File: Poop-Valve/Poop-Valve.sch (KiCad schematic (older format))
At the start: 51 parts, among them J1 RaspberryPi, J10 Valve Sig, J11 Conn_01x02_Male, J12 Relays, J13 LEDs, J14 24VDC, J15 Sensor, J16 Grove LCD, J2 Valve, J3 Charger, J4 Override, J5 Ovr Switch, J6 Power, J7 12VDC, J8 Conn_01x02_Male, J9 Conn_01x02_Male, K1 Override Relays, K2 Polarity Reverse, K3 Enable Relays, K4 Relay_Module, K5 Direction Relays, K6 Polarity Reverse, Q1 2N2222, Q2 2N2222, SW1 Override, SW2 Emergency Override, SW2 SW_DPDT_x2, SW3 Open/Close, U1 Opened, U2 Closed, U3 Override, U4 MCP3008

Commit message: v1.1 replace valve connector
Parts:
- removed J2: Valve, symbol Connector:6P6C
- added J17: Valve, symbol Connector:Conn_01x05_Male
- added J2: Dongle, symbol Connector:Conn_01x05_Female
- J10: value Valve Sig -> O/C
- gave numbers to parts that had none: 1
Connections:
- net +12V: now reaches F1.2, J11.1 (Pin_1), J8.1 (Pin_1), J9.1 (Pin_1), K5.~ (VCC), K6.~ (VCC), SW2.3, SW3.1
- net +12V: now also J10.2 (Pin_2), J17.3 (Pin_3)
- net at R3.2, R6.2: now also J10.1 (Pin_1), J17.2 (Pin_2); no longer J10.3 (Pin_3)
- net at R2.2, R5.2: now also J10.3 (Pin_3), J17.1 (Pin_1); no longer J10.1 (Pin_1)
- new net: K1.~ (VCC), K2.~ (VCC), K3.~ (VCC), K4.~ (VCC), K5.~ (VCC), K6.~ (VCC)
- new net: K1.~ (VCC), K3.~ (VCC)
- new net: K3.~ (VCC), K6.~ (VCC)
- new net: K2.~ (VCC), K4.~ (VCC)
- new net: K4.~ (VCC), K5.~ (VCC)
- new net: J17.5 (Pin_5), K1.~ (VCC)
- new net: J17.4 (Pin_4), K2.~ (VCC)
- no-connect marks 36 -> 33
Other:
- note added: "Ovr"
- note added: "Run"
- note added: "SW2\nEmergency\nOverride"
- note added: "To valve"
- note added: "black/white"
- note removed: "Operate"
- note removed: "Override"
- note removed: "pin"
- moved on the sheet: J16

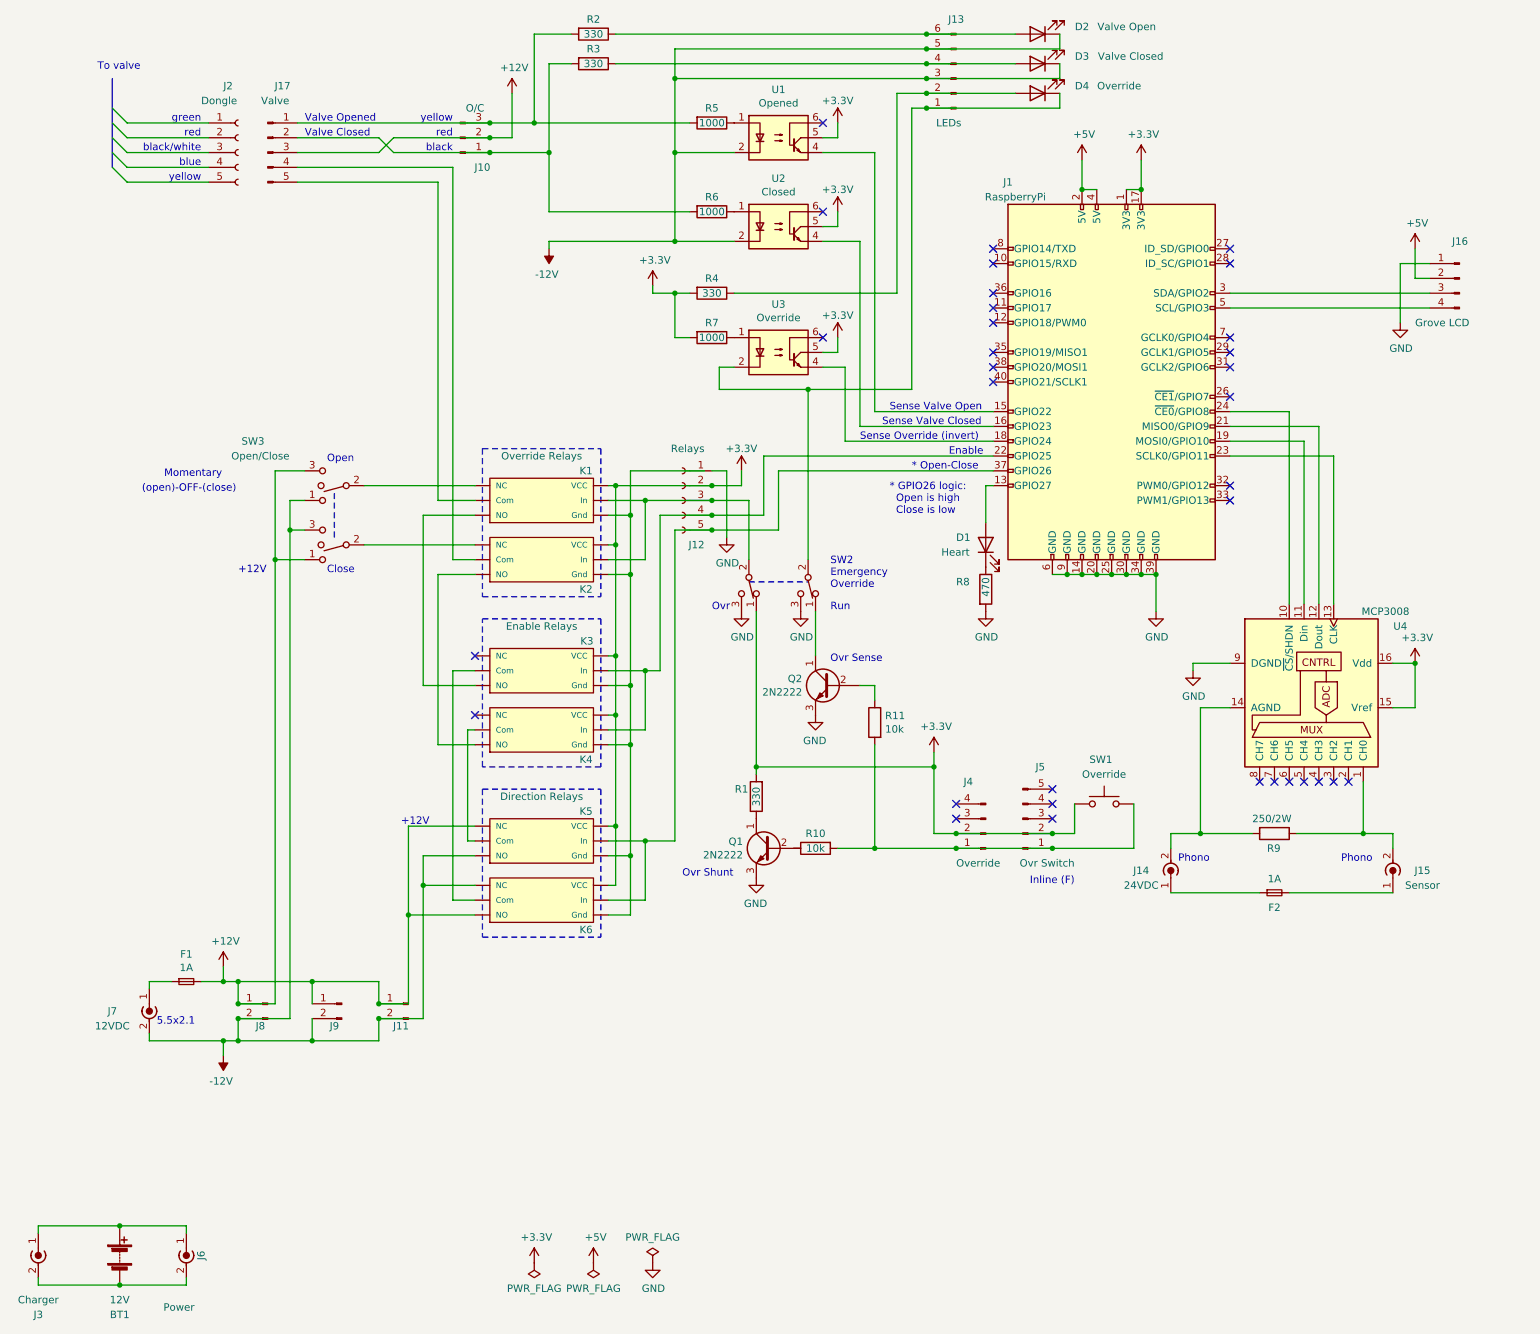
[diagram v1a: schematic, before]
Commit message: v1.2 reconfigure override relay to use 5V voltage divider; renumber parts; miscellaneous cosmetic cleanups
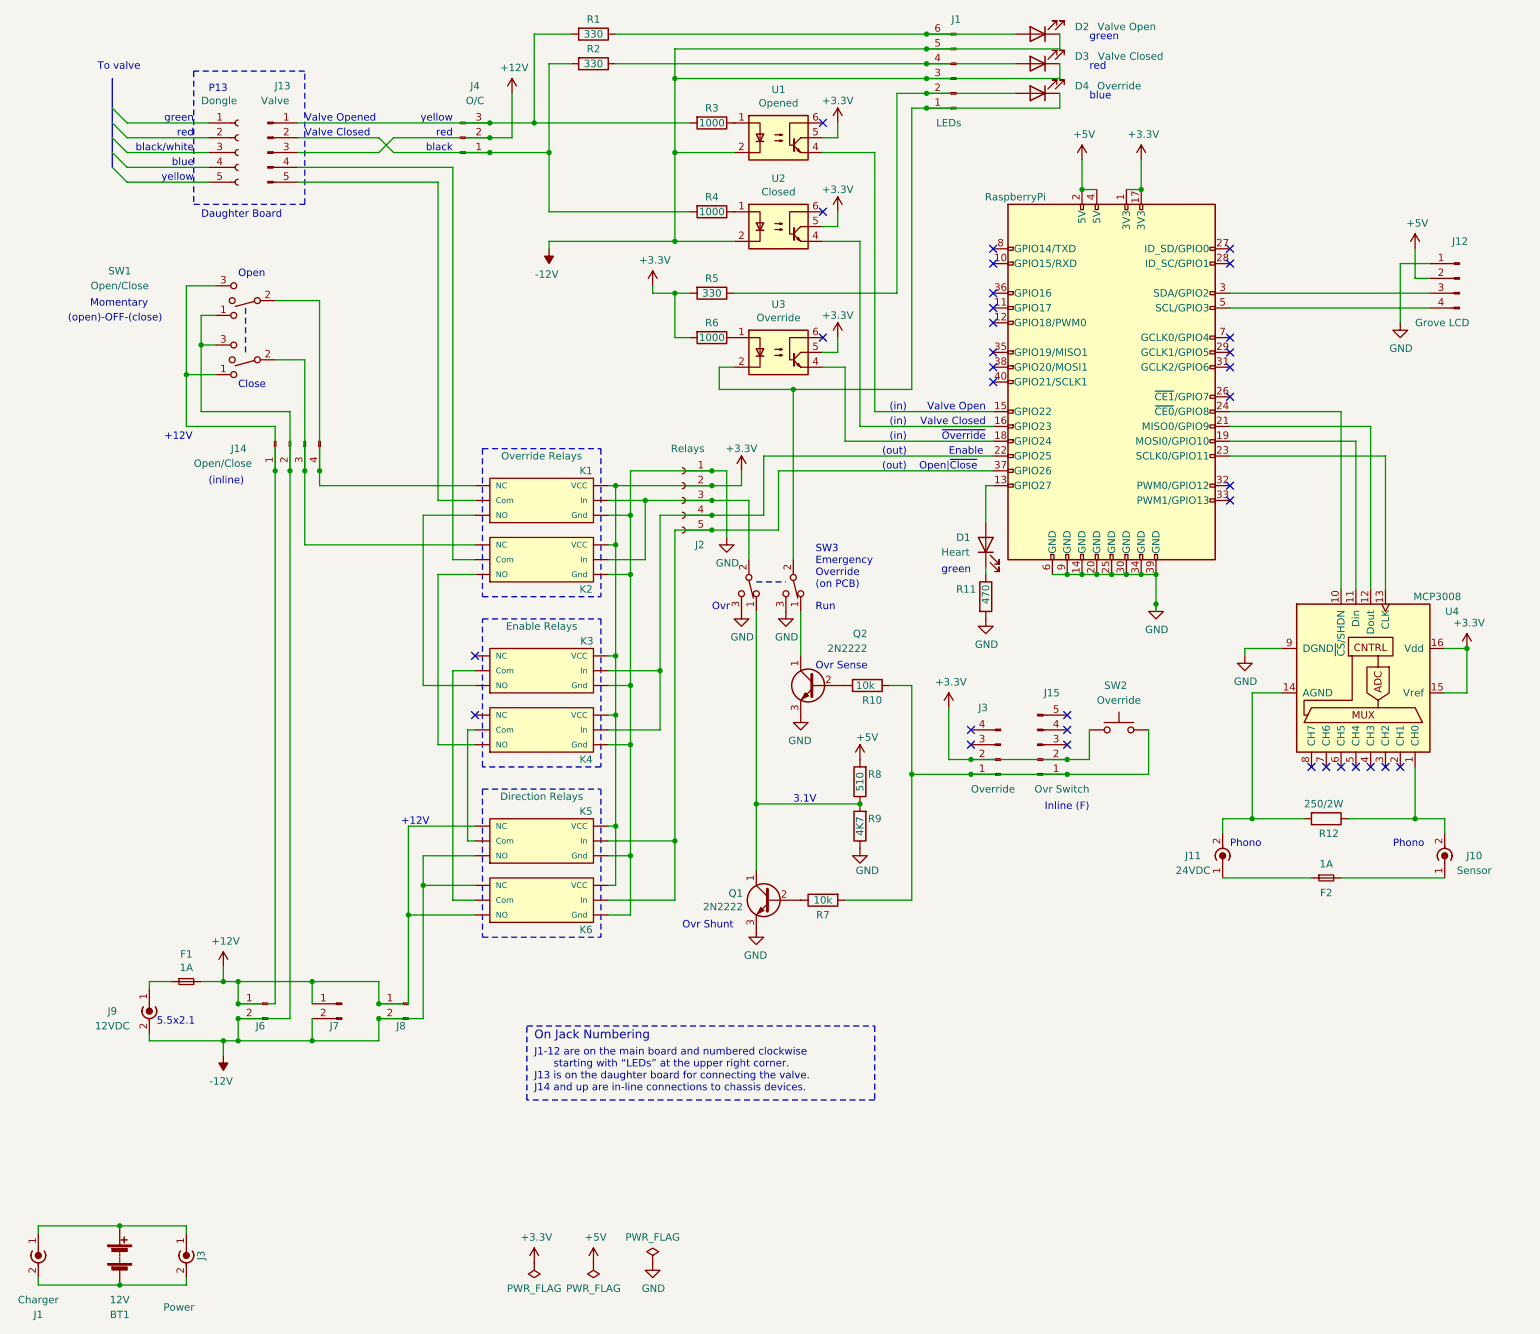
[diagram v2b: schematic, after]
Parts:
- added J14: Open/Close, symbol Connector:Conn_01x04_Male
- added R9: 4K7, symbol Device:R
- R8: renamed from R1; value 330 -> 510
- renumbered J3 to J1, J13 to J1, J15 to J10, J14 to J11, J16 to J12, J17 to J13, J5 to J15, J12 to J2, J6 to J3, J4 to J3, J10 to J4, J2 to J4, J8 to J6, J9 to J7, J11 to J8, J7 to J9, J1 to J99, R2 to R1, R11 to R10, R8 to R11, R9 to R12, R3 to R2, R5 to R3, R6 to R4, R4 to R5, R7 to R6, R10 to R7, SW3 to SW1, SW2 to SW1b1, SW1 to SW2, SW4 to SW3A1, SW2 to SW3B1
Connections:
- net +12V: now also J14.1 (Pin_1)
- net +3V3: no longer R8.2, SW3A1.1 (A)
- net +5V: now also R8.2
- net -12V: now also J14.2 (Pin_2)
- net GND: now also K1.~ (VCC), K2.~ (VCC), K3.~ (VCC), K4.~ (VCC), K5.~ (VCC), K6.~ (VCC), R9.1
- net at J15.1 (Pin_1), J3.1 (Pin_1), R7.2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: now also R10.1; no longer R10.2
- net at K1.~ (VCC), SW1b1.2: now also J14.4 (Pin_4)
- net at K2.~ (VCC), SW1.2: now also J14.3 (Pin_3)
- net at Q1.1 (C), R8.1: now also SW3A1.1 (A), R9.2
- net at Q1.2 (B): now also R7.1
- net at Q2.2 (B): now also R10.2; no longer R10.1
- new net: K1.~ (VCC), K3.~ (VCC)
- new net: K3.~ (VCC), K6.~ (VCC)
- new net: K2.~ (VCC), K4.~ (VCC)
- new net: K4.~ (VCC), K5.~ (VCC)
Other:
- note added: "(in)"
- note added: "(inline)"
- note added: "(out)"
- note added: "3.1V"
- note added: "Daughter Board"
- note added: "J1-12 are on the main board and numbered clockwise\n starting with “LEDs” at the upper right corner.\nJ13 is on the daughter board for connecting the valve.\nJ14 and up are in-line connections to chassis devices."
- note added: "On Jack Numbering"
- note added: "Open|~Close"
- note added: "P13"
- note added: "SW3\nEmergency\nOverride\n(on PCB)"
- note added: "Valve Closed\n"
- note added: "Valve Open"
- note added: "~Override"
- note removed: "* GPIO26 logic:\n Open is high\n Close is low"
- note removed: "* Open-Close"
- note removed: "SW2\nEmergency\nOverride"
- note removed: "Sense Override (invert)"
- note removed: "Sense Valve Closed\n"
- note removed: "Sense Valve Open"
- moved on the sheet: F2, J10, J11, J15, J3, Q1, Q2, R10, R11, R12, R7, R8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
